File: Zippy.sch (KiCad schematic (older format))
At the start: 5 parts, among them J1 USB_C_Receptacle_USB2.0, SW1 SW_Push, U1 Z80CPU, X1 GR-8002DC-PTB

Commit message: Committing the basics.
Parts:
- added C1, C2: 10pF, symbol Device:C_Small
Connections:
- net labels added: CLK, D[0..8]
- wire segments 42 -> 57
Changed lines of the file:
@@
 EESchema Schematic File Version 4
-LIBS:Zippy-cache
-EELAYER 26 0
+EELAYER 30 0
 EELAYER END
 $Descr A4 11693 8268
 encoding utf-8
-Sheet 1 2
+Sheet 1 3
 Title ""
 Date ""
@@
 NoConn ~ 2650 4200
 $Comp
-L power:GND #PWR07
+L power:GND #PWR05
 U 1 1 5D7EF90F
 P 2650 4400
-F 0 "#PWR07" H 2650 4150 50  0001 C CNN
+F 0 "#PWR05" H 2650 4150 50  0001 C CNN
 F 1 "GND" V 2655 4272 50  0000 R CNN
 F 2 "" H 2650 4400 50  0001 C CNN
@@
 $EndComp
 $Comp
-L power:+5V #PWR010
+L power:+5V #PWR011
 U 1 1 5D7EFCCD
 P 4000 1900
-F 0 "#PWR010" H 4000 1750 50  0001 C CNN
+F 0 "#PWR011" H 4000 1750 50  0001 C CNN
 F 1 "+5V" H 4015 2073 50  0000 C CNN
 F 2 "" H 4000 1900 50  0001 C CNN
@@
 $EndComp
 $Comp
-L power:GND #PWR04
+L power:GND #PWR02
 U 1 1 5D7EFE58
 P 2500 900
-F 0 "#PWR04" H 2500 650 50  0001 C CNN
+F 0 "#PWR02" H 2500 650 50  0001 C CNN
 F 1 "GND" V 2505 772 50  0000 R CNN
 F 2 "" H 2500 900 50  0001 C CNN
@@
 $EndComp
 $Comp
-L power:GND #PWR05
+L power:GND #PWR03
 U 1 1 5D7EFECB
 P 2500 1200
-F 0 "#PWR05" H 2500 950 50  0001 C CNN
+F 0 "#PWR03" H 2500 950 50  0001 C CNN
 F 1 "GND" V 2505 1072 50  0000 R CNN
 F 2 "" H 2500 1200 50  0001 C CNN
@@
 NoConn ~ 3800 1800
 $Comp
-L power:+5V #PWR06
+L power:+5V #PWR04
 U 1 1 5D7F7F3A
 P 2500 2700
-F 0 "#PWR06" H 2500 2550 50  0001 C CNN
+F 0 "#PWR04" H 2500 2550 50  0001 C CNN
 F 1 "+5V" H 2515 2873 50  0000 C CNN
 F 2 "" H 2500 2700 50  0001 C CNN
@@
 L power:+5V #PWR08
 U 1 1 5D7F8146
-P 3350 2800
-F 0 "#PWR08" H 3350 2650 50  0001 C CNN
-F 1 "+5V" H 3365 2973 50  0000 C CNN
-F 2 "" H 3350 2800 50  0001 C CNN
-F 3 "" H 3350 2800 50  0001 C CNN
-	1    3350 2800
+P 3350 2600
+F 0 "#PWR08" H 3350 2450 50  0001 C CNN
+F 1 "+5V" H 3365 2773 50  0000 C CNN
+F 2 "" H 3350 2600 50  0001 C CNN
+F 3 "" H 3350 2600 50  0001 C CNN
+	1    3350 2600
 	1    0    0    -1
 $EndComp
@@
 	4000 1800 4000 1850
 $Comp
-L power:PWR_FLAG #FLG0101
+L power:PWR_FLAG #FLG01
 U 1 1 5D7F220C
 P 4000 1850
-F 0 "#FLG0101" H 4000 1925 50  0001 C CNN
+F 0 "#FLG01" H 4000 1925 50  0001 C CNN
 F 1 "PWR_FLAG" V 4000 1978 50  0000 L CNN
 F 2 "" H 4000 1850 50  0001 C CNN
@@
 	4000 1850 4000 1900
 $Sheet
-S 9650 650  1400 150
+S 7250 850  1250 850
 U 5D7F3F15
 F0 "Zippy Crowbar Backplane" 50
 F1 "crowbar-backplane.sch" 50
+F2 "~RD" I L 7250 1200 50
+F3 "~MREQ" I L 7250 1300 50
+F4 "~INT" I L 7250 1400 50
+F5 "~M1" I L 7250 1600 50
+F6 "D[0..8]" I L 7250 1050 50
+F7 "A[0..15]" I R 8500 1050 50
+F8 "CLK" I L 7250 900 50
+F9 "~WR" I R 8500 1200 50
+F10 "~IORQ" I R 8500 1300 50
+F11 "~NMI" I R 8500 1400 50
+F12 "~BUSACK" I R 8500 1500 50
+F13 "~WAIT" I R 8500 1600 50
+F14 "~BUSRQ" I L 7250 1500 50
 $EndSheet
 $Comp
@@
 $EndComp
 $Comp
-L power:GND #PWR013
+L power:GND #PWR010
 U 1 1 5D7F2CC9
 P 3900 7000
-F 0 "#PWR013" H 3900 6750 50  0001 C CNN
+F 0 "#PWR010" H 3900 6750 50  0001 C CNN
 F 1 "GND" H 3905 6827 50  0000 C CNN
 F 2 "" H 3900 7000 50  0001 C CNN
@@
 $EndComp
 $Comp
-L power:+5V #PWR011
+L power:+5V #PWR06
 U 1 1 5D7F2DD8
-P 2800 6700
-F 0 "#PWR011" H 2800 6550 50  0001 C CNN
-F 1 "+5V" H 2815 6873 50  0000 C CNN
-F 2 "" H 2800 6700 50  0001 C CNN
-F 3 "" H 2800 6700 50  0001 C CNN
-	1    2800 6700
+P 2600 6700
+F 0 "#PWR06" H 2600 6550 50  0001 C CNN
+F 1 "+5V" H 2615 6873 50  0000 C CNN
+F 2 "" H 2600 6700 50  0001 C CNN
+F 3 "" H 2600 6700 50  0001 C CNN
+	1    2600 6700
 	0    -1   -1   0
 $EndComp
 $Comp
-L power:+5V #PWR012
+L power:+5V #PWR07
 U 1 1 5D7F2EC9
 P 2800 7000
-F 0 "#PWR012" H 2800 6850 50  0001 C CNN
+F 0 "#PWR07" H 2800 6850 50  0001 C CNN
 F 1 "+5V" H 2815 7173 50  0000 C CNN
 F 2 "" H 2800 7000 50  0001 C CNN
@@
 Wire Wire Line
 	3900 6700 4100 6700
-Text Label 4550 2950 0    50   ~ 0
+Text Label 4550 3000 0    50   ~ 0
 A[0..15]
-Text Label 4550 5700 0    50   ~ 0
+Text Label 4550 5650 0    50   ~ 0
 D[0..7]
+Wire Wire Line
+	7250 900  6850 900
+Wire Wire Line
+	7250 1200 6850 1200
+Wire Wire Line
+	7250 1300 6850 1300
+Wire Wire Line
+	7250 1400 6850 1400
+Wire Wire Line
+	7250 1500 6850 1500
+Wire Wire Line
+	7250 1600 6850 1600
+Wire Wire Line
+	8900 1200 8500 1200
+Wire Wire Line
+	8900 1300 8500 1300
+Wire Wire Line
+	8900 1400 8500 1400
+Wire Wire Line
+	8900 1500 8500 1500
+Wire Wire Line
+	8900 1600 8500 1600
+Text Label 6850 900  0    50   ~ 0
+CLK
+Wire Bus Line
+	7250 1050 6850 1050
+Wire Bus Line
+	8500 1050 8900 1050
+Text Label 6850 1050 0    50   ~ 0
+D[0..8]
+Text Label 8900 1050 2    50   ~ 0
+A[0..15]
+Text Label 6850 1200 0    50   ~ 0
+~RD
+Text Label 6850 1300 0    50   ~ 0
+~MREQ
+Text Label 6850 1400 0    50   ~ 0
+~INT
+Text Label 6850 1500 0    50   ~ 0
+~BUSRQ
+Text Label 6850 1600 0    50   ~ 0
+~M1
+Text Label 8900 1200 2    50   ~ 0
+~WR
+Text Label 8900 1300 2    50   ~ 0
+~IORQ
+Text Label 8900 1400 2    50   ~ 0
+~NMI
+Text Label 8900 1500 2    50   ~ 0
+~BUSACK
+Text Label 8900 1600 2    50   ~ 0
+~WAIT
+$Comp
+L Device:C_Small C1
+U 1 1 5D94779F
+P 3350 2700
+F 0 "C1" H 3442 2746 50  0000 L CNN
+F 1 "10pF" H 3442 2655 50  0000 L CNN
+F 2 "" H 3350 2700 50  0001 C CNN
+F 3 "~" H 3350 2700 50  0001 C CNN
+	1    3350 2700
+	1    0    0    -1
+$EndComp
+$Comp
+L Device:C_Small C2
+U 1 1 5D948512
+P 2700 6700
+F 0 "C2" V 2471 6700 50  0000 C CNN
+F 1 "10pF" V 2562 6700 50  0000 C CNN
+F 2 "" H 2700 6700 50  0001 C CNN
+F 3 "~" H 2700 6700 50  0001 C CNN
+	1    2700 6700
+	0    1    1    0
+$EndComp
+$Sheet
+S 7250 2250 1250 800
+U 5D949038
+F0 "Serial Connectivity" 50
+F1 "serial-connectivity.sch" 50
+F2 "A[0..15]" I R 8500 2400 50
+F3 "D[0..8]" I L 7250 2400 50
+F4 "~WAIT" I L 7250 2550 50
+F5 "~IORQ" I R 8500 2550 50
+F6 "~RD" I L 7250 2650 50
+F7 "~WR" I R 8500 2650 50
+$EndSheet
+Wire Bus Line
+	7250 2400 6850 2400
+Text Label 6850 2400 0    50   ~ 0
+D[0..8]
+Wire Bus Line
+	8500 2400 8900 2400
+Text Label 8900 2400 2    50   ~ 0
+A[0..15]
+Wire Wire Line
+	6850 2550 7250 2550
+Text Label 6850 2550 0    50   ~ 0
+~WAIT
+Wire Wire Line
+	6850 2650 7250 2650
+Text Label 6850 2650 0    50   ~ 0
+~RD
+Wire Wire Line
+	8900 2550 8500 2550
+Text Label 8900 2550 2    50   ~ 0
+~IORQ
+Wire Wire Line
+	8900 2650 8500 2650
+Text Label 8900 2650 2    50   ~ 0
+~WR
 Wire Bus Line
 	4550 4900 4550 5700

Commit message: Import of the major redesign and most of the schematic.
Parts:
- removed C1, C2: 10pF, symbol Device:C_Small
- removed J1: USB_C_Receptacle_USB2.0, symbol Connector:USB_C_Receptacle_USB2.0
- removed R1: 1K, symbol Device:R_Small_US
- removed SW1: SW_Push, symbol Switch:SW_Push
- removed U1: Z80CPU, symbol CPU:Z80CPU
- removed X1: GR-8002DC-PTB, symbol Zippy:GR-8002DC-PTB
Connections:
- net labels removed: +5V, A0, A1, A10, A11, A12, A13, A14, A15, A2, A3, A4, A5, A6, A7, A8, A9, A[0..15], CLK, D0, D1, D2, D3, D4, D5, D6, D7, D[0..7], D[0..8], GND, ~BUSACK, ~BUSRQ, ~CLK, ~INT, ~IORQ, ~M1, ~MREQ, ~NMI, ~RD, ~WAIT, ~WR
- wire segments 57 -> 0
- no-connect marks 9 -> 0

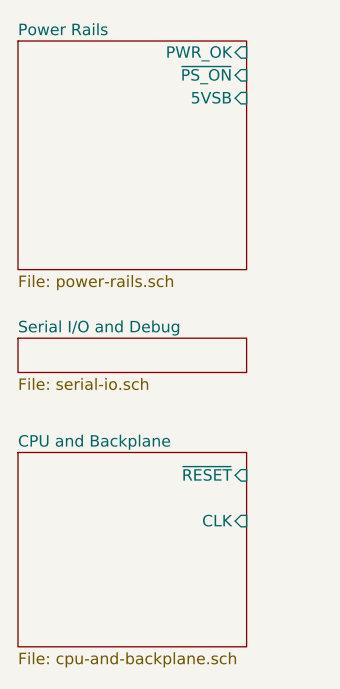
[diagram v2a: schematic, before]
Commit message: Crowbar updates and ERC fixes
This updates the Crowbar bus connectors and the layout of the
schematic to match the finalized pinouts. It also corrects an
error in the original schematic where the buses were not
properly routing due to lack of labels.

Finally, this change includes fixes for the ERC and adds the CPU
and RTC crystals to the system.
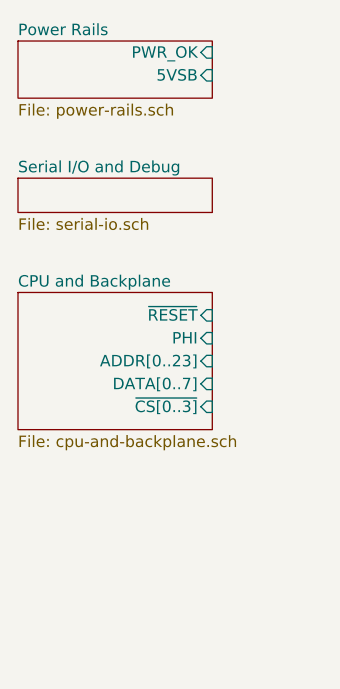
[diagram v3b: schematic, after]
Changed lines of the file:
@@
 EESchema Schematic File Version 4
+LIBS:Zippy-cache
 EELAYER 29 0
 EELAYER END
@@
 $EndDescr
 $Sheet
-S 650  2500 1000 850
+S 650  1800 850  600
 U 5D7F3F15
 F0 "CPU and Backplane" 50
 F1 "cpu-and-backplane.sch" 50
-F2 "~RESET" I R 1650 2600 50
-F3 "CLK" I R 1650 2800 50
+F2 "~RESET" I R 1500 1900 50
+F3 "PHI" I R 1500 2000 50
+F4 "ADDR[0..23]" I R 1500 2100 50
+F5 "DATA[0..7]" I R 1500 2200 50
+F6 "~CS[0..3]" I R 1500 2300 50
 $EndSheet
 $Sheet
-S 650  700  1000 1000
+S 650  700  850  250
 U 5D86D88B
 F0 "Power Rails" 50
 F1 "power-rails.sch" 50
-F2 "PWR_OK" I R 1650 750 50
-F3 "~PS_ON" I R 1650 850 50
-F4 "5VSB" I R 1650 950 50
+F2 "PWR_OK" I R 1500 750 50
+F3 "5VSB" I R 1500 850 50
 $EndSheet
 $Sheet
-S 650  2000 1000 150
+S 650  1300 850  150
 U 5DA1EBE5
 F0 "Serial I/O and Debug" 50

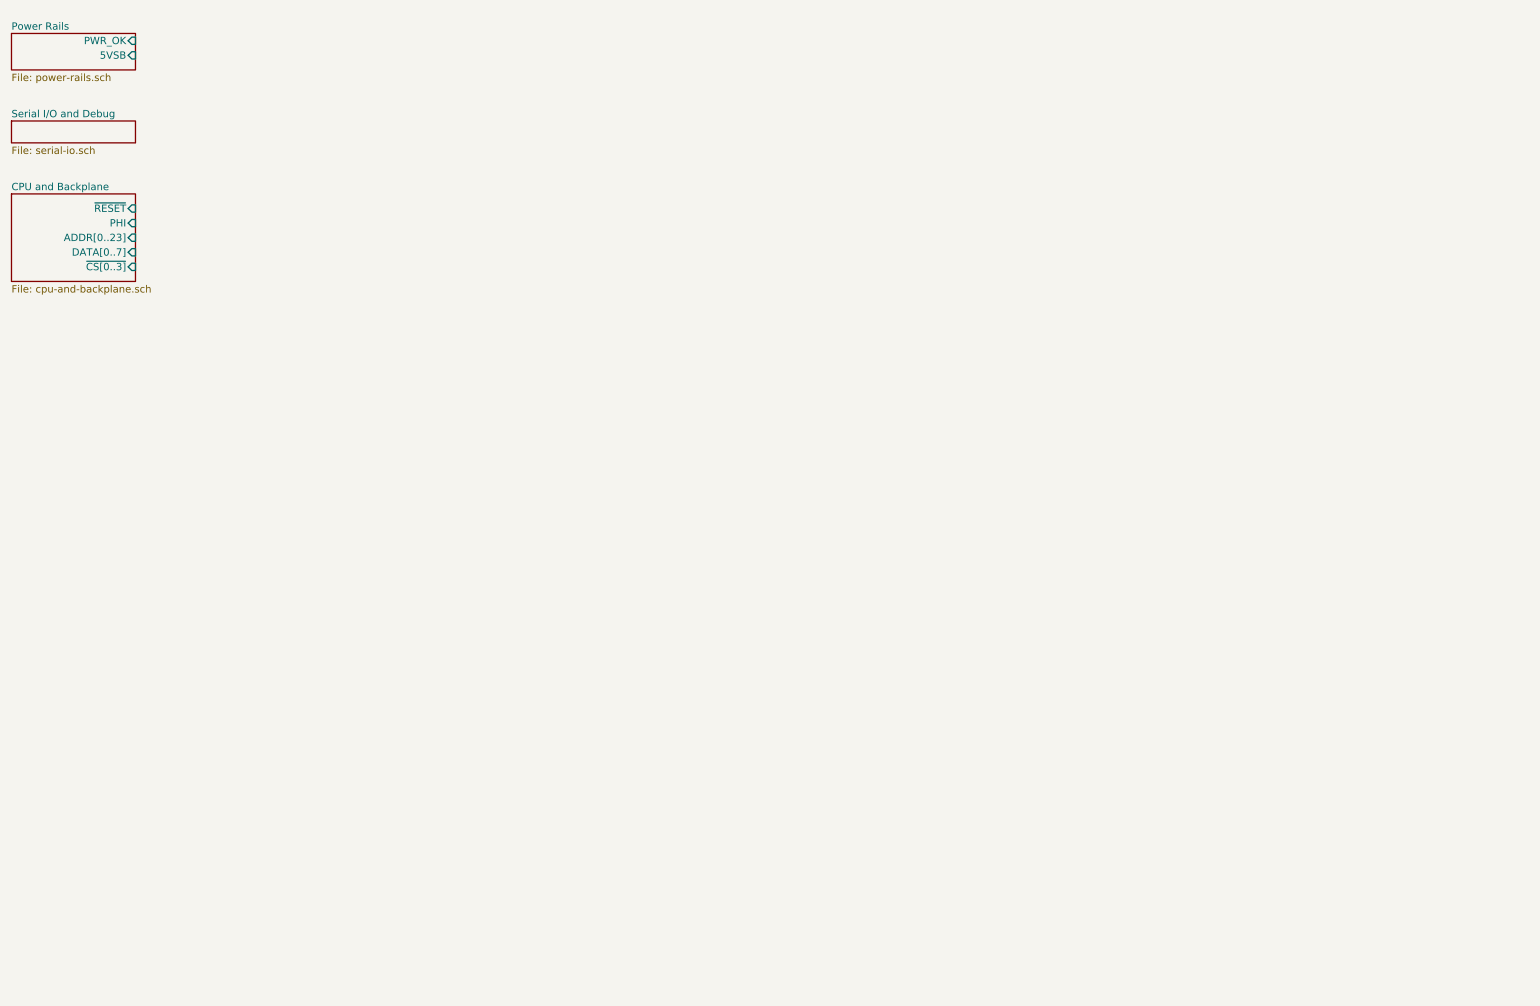
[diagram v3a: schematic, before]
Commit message: System management, serial I/O, and power refinement
  - Swapped the XTAL for the CPU to the programmable OSC.
  - Cleaned up the decoupling caps according to datasheets
    and "rule of thumb" experimental results in
    https://www.edn.com/design/components-and-packaging/4351231/EDN-Access-09-01-95-Don-t-let-rules-of-thumb-set-decoupling-capacitor-value
  - Added an ATMega328 for use as a system management uC.
    Primarily used for soft power on/off of the ATX PSU
    and control the state of /RESET during power on.
  - Reorganized the top level sheet to better illustrate
    the relationships between sheets.
  - Added an additional FT232 USB->UART IC for use with
    the SMC uC.
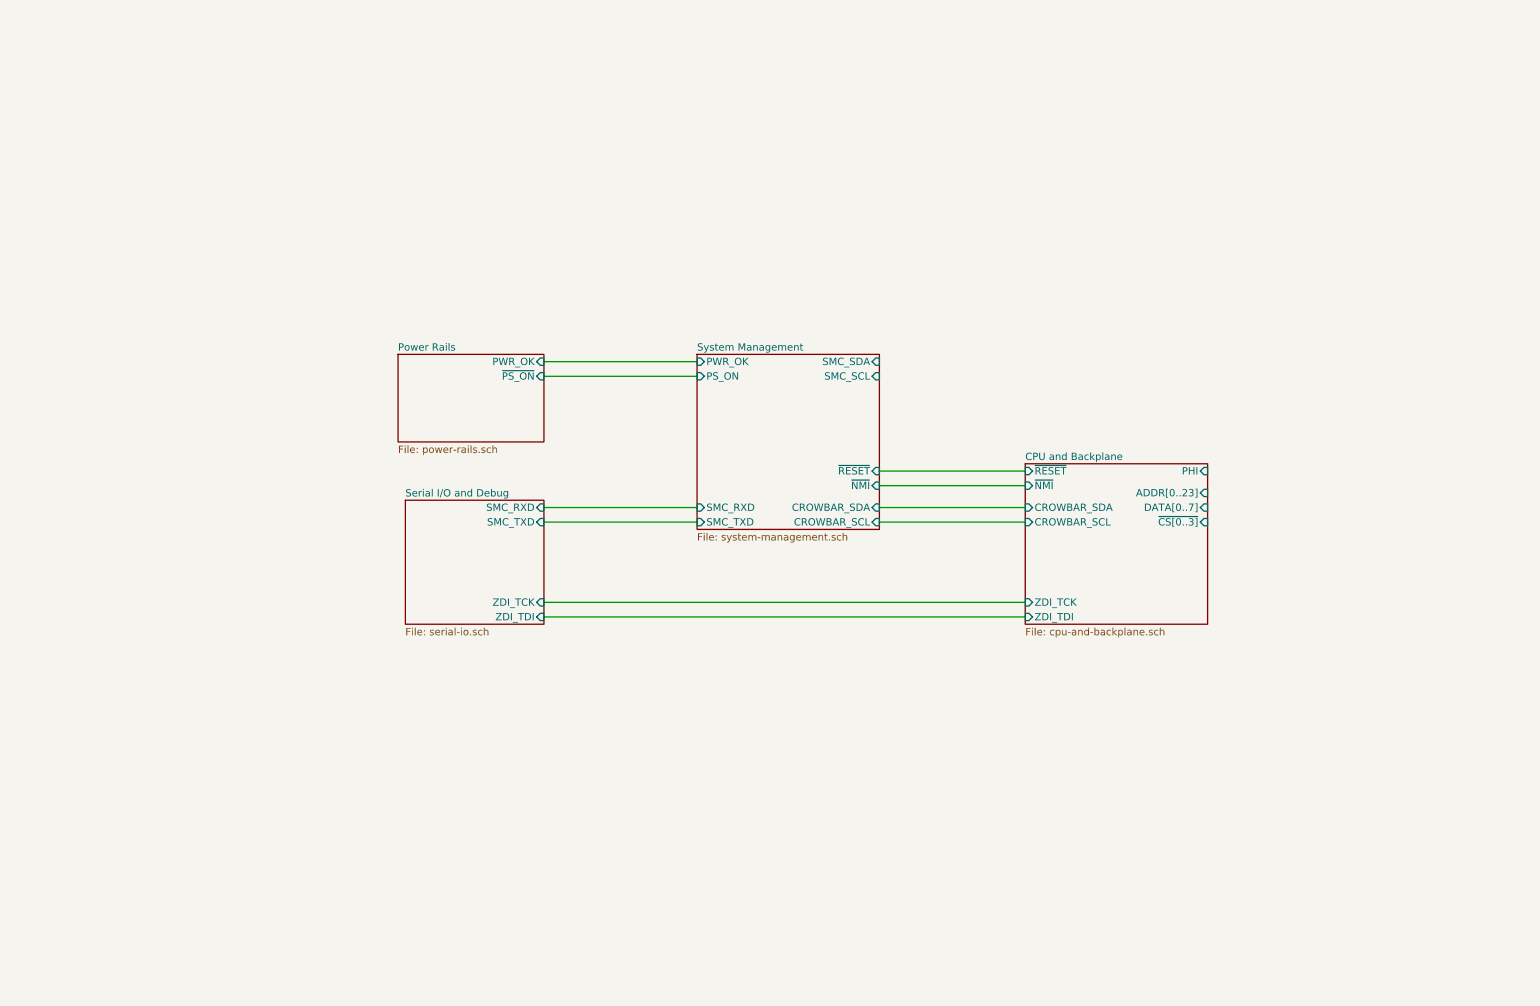
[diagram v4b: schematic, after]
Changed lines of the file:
@@
 $Descr A4 11693 8268
 encoding utf-8
-Sheet 1 5
+Sheet 1 6
 Title ""
 Date ""
@@
 $EndDescr
 $Sheet
-S 650  1800 850  600
+S 7600 3650 1250 1100
 U 5D7F3F15
 F0 "CPU and Backplane" 50
 F1 "cpu-and-backplane.sch" 50
-F2 "~RESET" I R 1500 1900 50
-F3 "PHI" I R 1500 2000 50
-F4 "ADDR[0..23]" I R 1500 2100 50
-F5 "DATA[0..7]" I R 1500 2200 50
-F6 "~CS[0..3]" I R 1500 2300 50
+F2 "~RESET" I L 7600 3700 50
+F3 "PHI" I R 8850 3700 50
+F4 "ADDR[0..23]" I R 8850 3850 50
+F5 "DATA[0..7]" I R 8850 3950 50
+F6 "~CS[0..3]" I R 8850 4050 50
+F7 "ZDI_TCK" I L 7600 4600 50
+F8 "ZDI_TDI" I L 7600 4700 50
+F9 "~NMI" I L 7600 3800 50
+F10 "CROWBAR_SCL" I L 7600 4050 50
+F11 "CROWBAR_SDA" I L 7600 3950 50
 $EndSheet
 $Sheet
-S 650  700  850  250
+S 3300 2900 1000 600
 U 5D86D88B
 F0 "Power Rails" 50
 F1 "power-rails.sch" 50
-F2 "PWR_OK" I R 1500 750 50
-F3 "5VSB" I R 1500 850 50
+F2 "PWR_OK" I R 4300 2950 50
+F3 "~PS_ON" I R 4300 3050 50
 $EndSheet
 $Sheet
-S 650  1300 850  150
+S 5350 2900 1250 1200
+U 5D99435D
+F0 "System Management" 50
+F1 "system-management.sch" 50
+F2 "~RESET" I R 6600 3700 50
+F3 "PS_ON" I L 5350 3050 50
+F4 "SMC_RXD" I L 5350 3950 50
+F5 "SMC_TXD" I L 5350 4050 50
+F6 "CROWBAR_SDA" I R 6600 3950 50
+F7 "CROWBAR_SCL" I R 6600 4050 50
+F8 "~NMI" I R 6600 3800 50
+F9 "SMC_SDA" I R 6600 2950 50
+F10 "SMC_SCL" I R 6600 3050 50
+F11 "PWR_OK" I L 5350 2950 50
+$EndSheet
+Wire Wire Line
+	4300 2950 5350 2950
+Wire Wire Line
+	4300 3050 5350 3050
+Wire Wire Line
+	4300 3950 5350 3950
+Wire Wire Line
+	4300 4050 5350 4050
+$Sheet
+S 3350 3900 950  850
 U 5DA1EBE5
 F0 "Serial I/O and Debug" 50
 F1 "serial-io.sch" 50
+F2 "ZDI_TCK" I R 4300 4600 50
+F3 "ZDI_TDI" I R 4300 4700 50
+F4 "SMC_TXD" I R 4300 4050 50
+F5 "SMC_RXD" I R 4300 3950 50
 $EndSheet
+Wire Wire Line
+	4300 4600 7600 4600
+Wire Wire Line
+	4300 4700 7600 4700
+Wire Wire Line
+	6600 3700 7600 3700
+Wire Wire Line
+	6600 3800 7600 3800
+Wire Wire Line
+	6600 3950 7600 3950
+Wire Wire Line
+	6600 4050 7600 4050
 $EndSCHEMATC
